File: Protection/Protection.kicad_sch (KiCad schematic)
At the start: 71 parts, among them J1 V_IN, J2 JST_02, J3 5V_IN, J4 V_OUT, J5 JST_07, J6 JST_02, Q1 2N3904, Q2 BT152-800R, Q3 2N3904, Q4 2N3904, Q5 2N3904, Q6 IRF1404/IRFB4110, Q8 IRF1404/IRFB4110, U1 TL431LP, U2 LM393, U3 TLP250

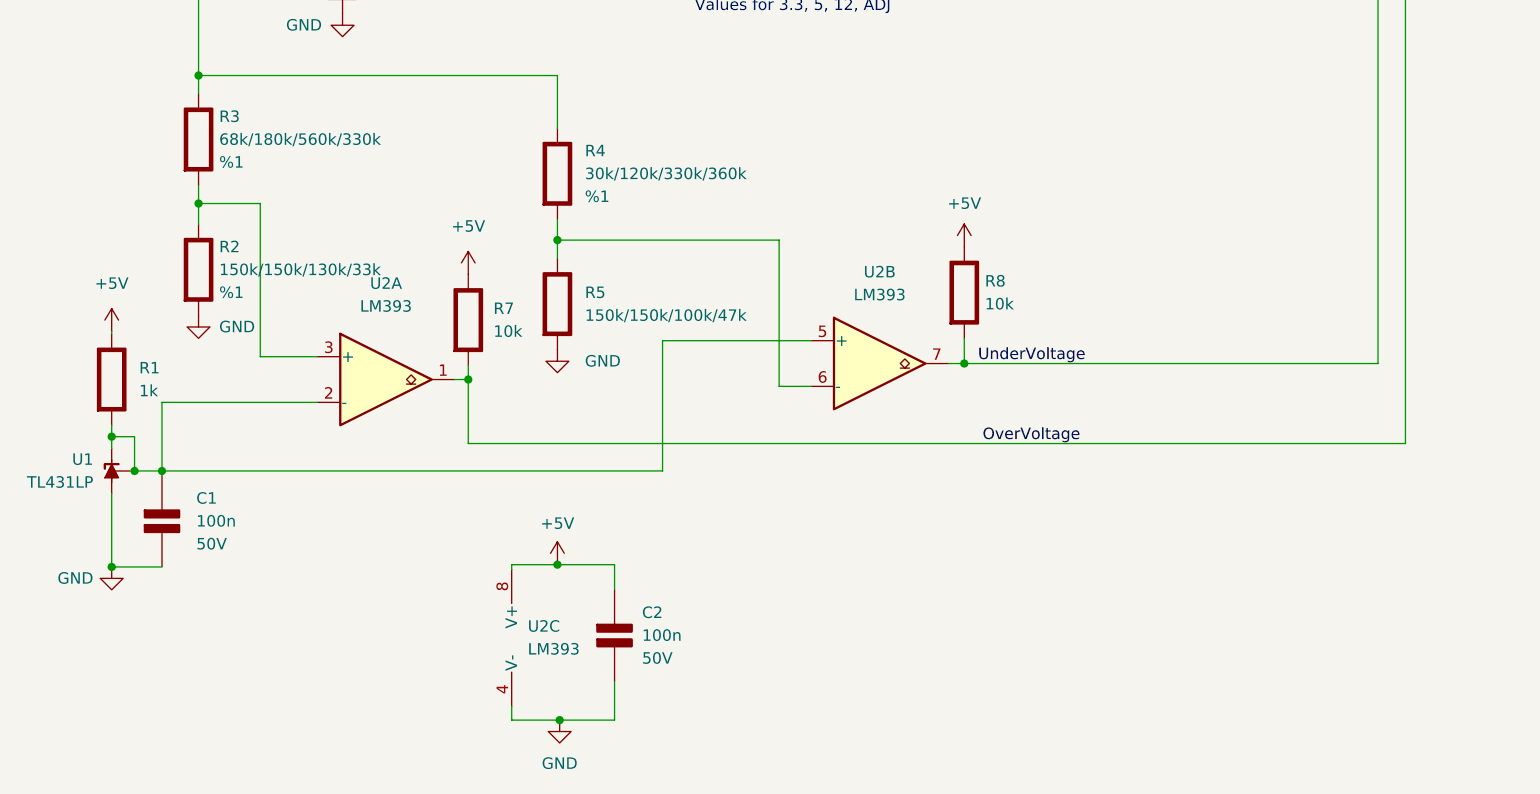
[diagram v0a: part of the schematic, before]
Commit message: Undervoltage protection fixed for adj ch
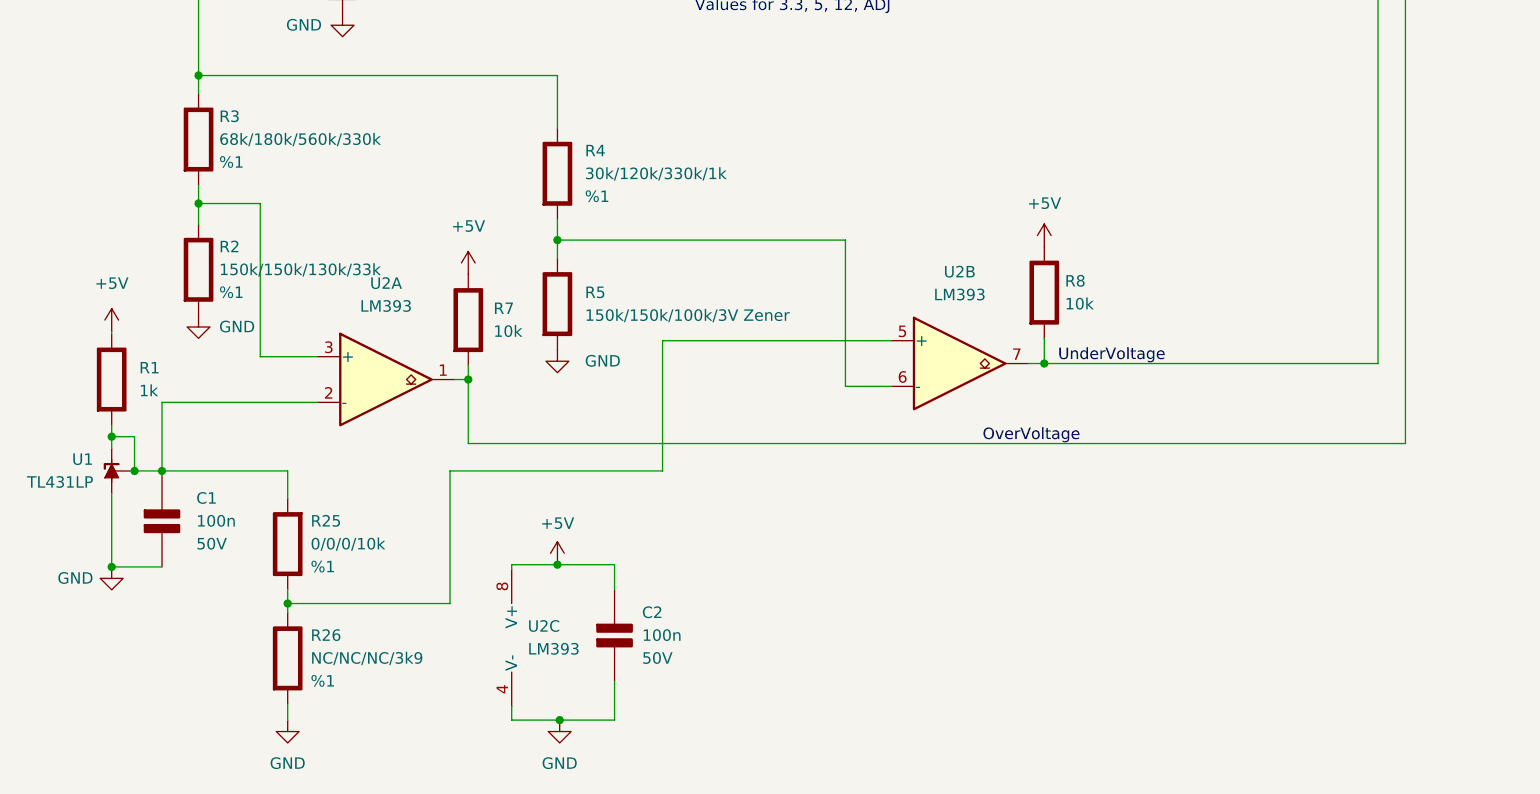
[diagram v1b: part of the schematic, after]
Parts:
- added R25: 0/0/0/10k, Resistor_THT:R_Axial_DIN0207_L6.3mm_D2.5mm_P10.16mm_Horizontal, symbol PCM_Elektuur:R
- added R26: NC/NC/NC/3k9, Resistor_THT:R_Axial_DIN0207_L6.3mm_D2.5mm_P10.16mm_Horizontal, symbol PCM_Elektuur:R
- R4: value 30k/120k/330k/360k -> 30k/120k/330k/1k
- R5: value 150k/150k/100k/47k -> 150k/150k/100k/3V Zener
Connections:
- net GND: now also R26.2 (-)
- net at C1.1 (+), R1.2 (-), U1.1 (REF)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: now also R25.2 (-); no longer U2.5 (+)
- new net: R25.1 (+), R26.1 (+), U2.5 (+)
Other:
- moved on the sheet: R8, U2B
